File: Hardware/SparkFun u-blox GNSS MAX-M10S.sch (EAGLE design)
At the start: 45 parts, among them J1 USB-to-Serial, J2 Qwiic RA, J3 PTH, J4 Qwiic RA, U1 MAX-M10S

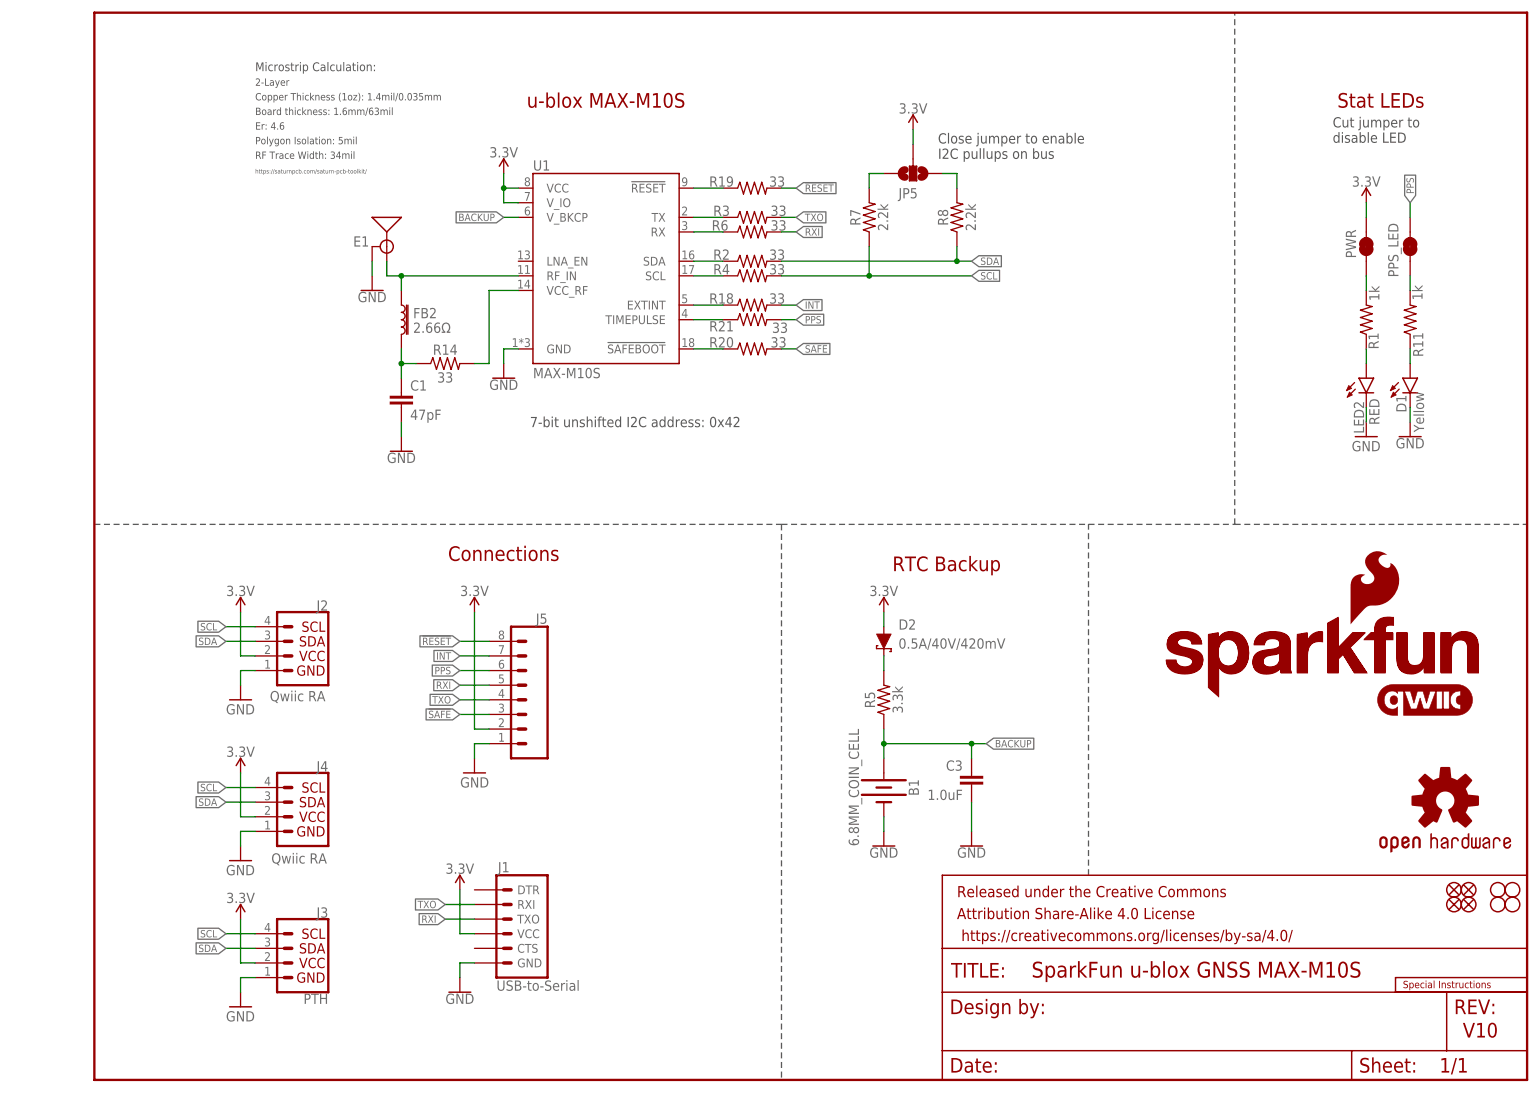
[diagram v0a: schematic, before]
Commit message: Changing RF path to 0402. Adding GND vias on both RF trace sides. Adding panel.
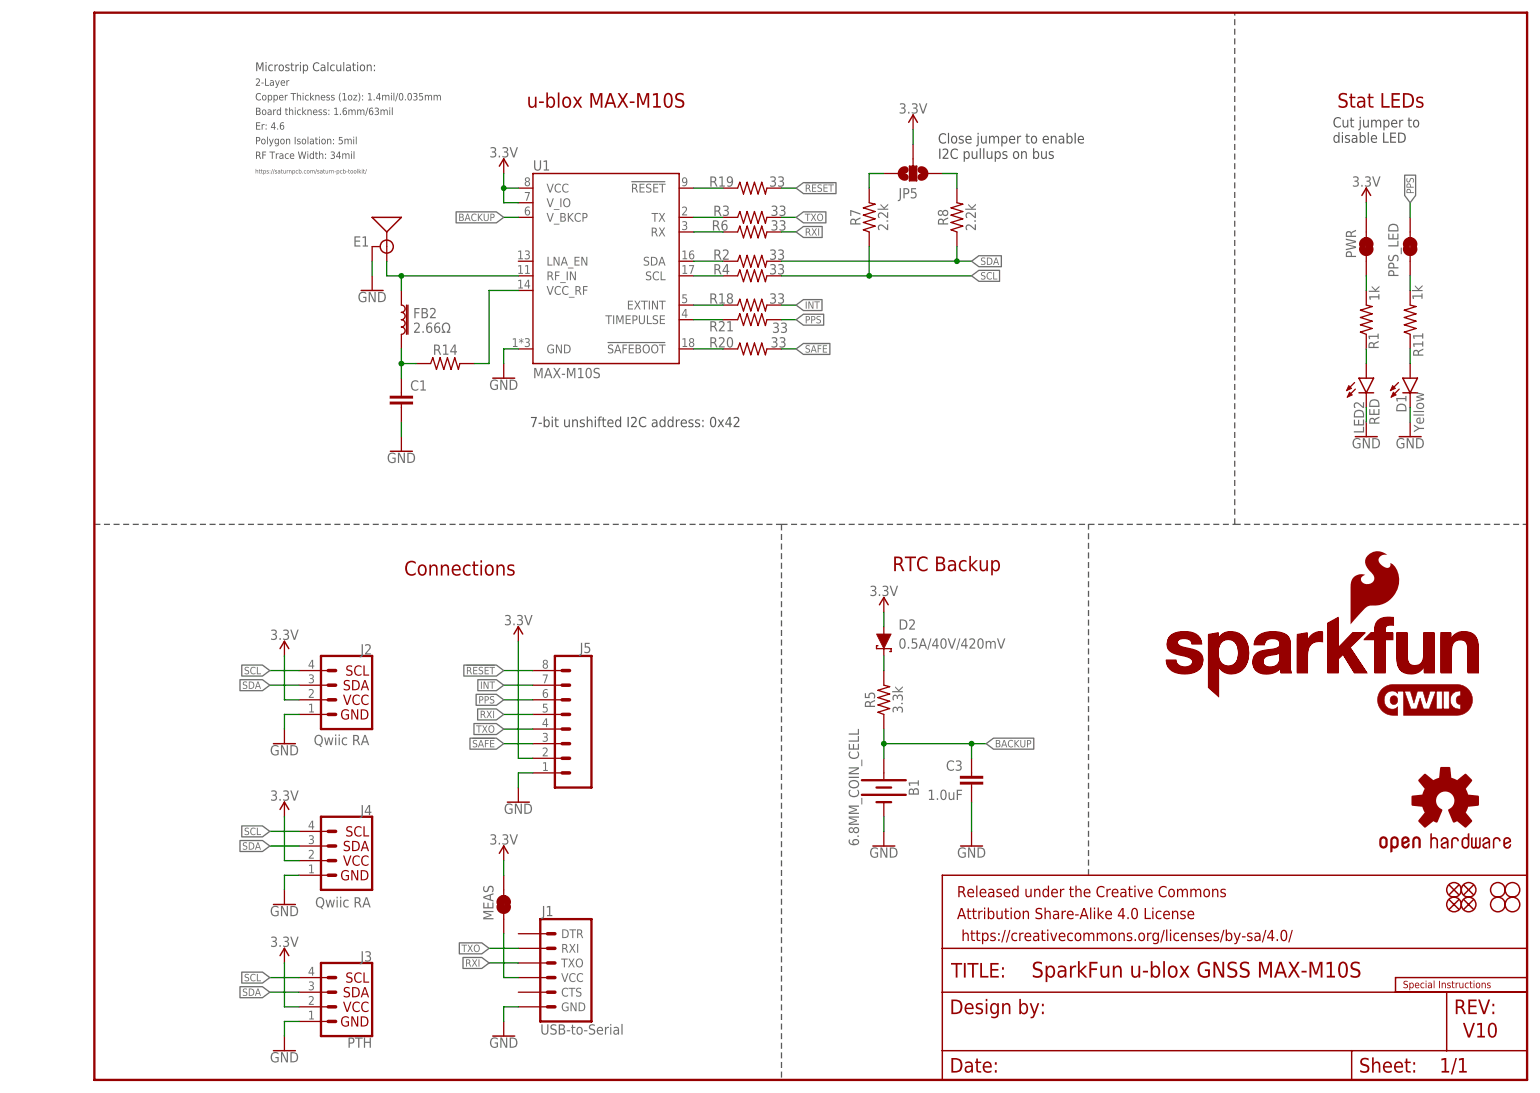
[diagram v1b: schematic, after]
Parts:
- added MEAS: JUMPER-COMBO_2_NC_TRACE, SparkFun-Jumpers:JUMPER-COMBO_2_NC_TRACE
- C1: value 47pF -> 47PF-0402_TIGHT-25V-5%-X7R; device SparkFun-Capacitors:47PF-0402-25V-5%-X7R -> SparkFun-Capacitors:47PF-0402_TIGHT-25V-5%-X7R
- R14: value 33 -> 33OHM-0402T-1/10W-1%; device SparkFun-Resistors:33OHM-0603-1/10W-1% -> SparkFun-Resistors:33OHM-0402T-1/10W-1%
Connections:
- new net N$1: J1.VCC, MEAS.1
- net 3.3V: now also MEAS.2; no longer J1.VCC
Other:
- moved on the sheet: J1, J2, J3, J4, J5

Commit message: Add ESD RF diode. Change to PTH SMA.
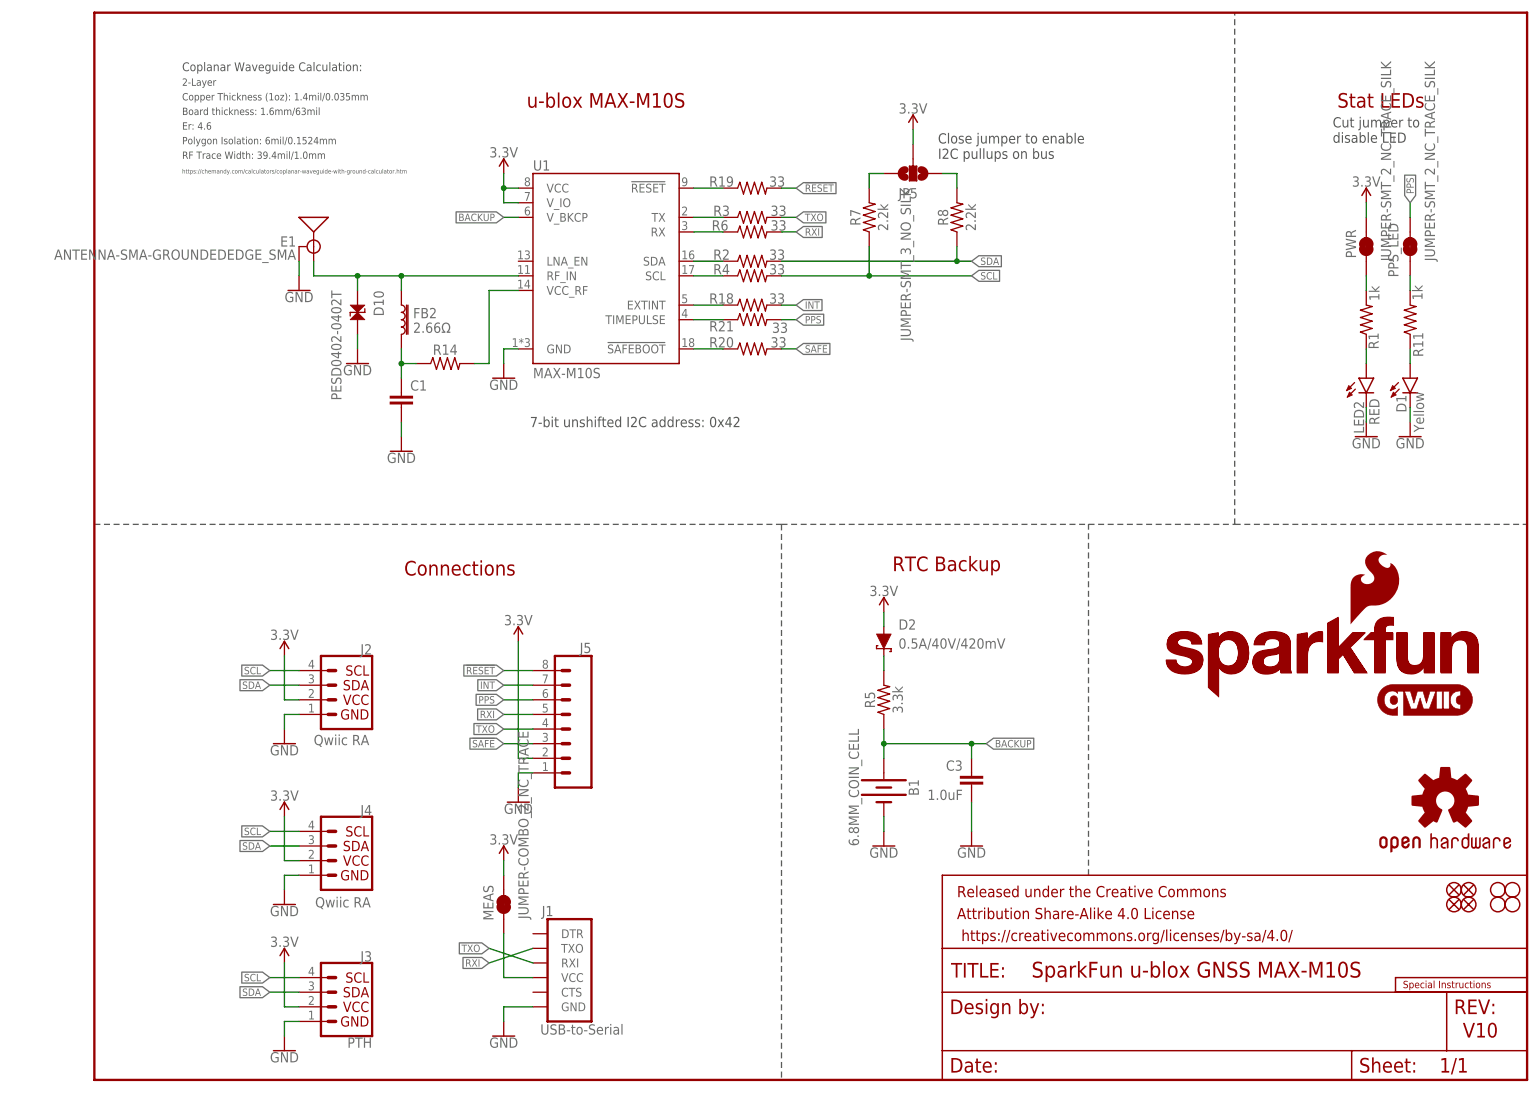
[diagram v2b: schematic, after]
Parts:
- added D10: PESD0402-0402T, SparkFun-DiscreteSemi:PESD0402-0402T
- C1: value 47PF-0402_TIGHT-25V-5%-X7R -> 47pF
- E1: value ANTENNA-SMA-GROUNDEDEDGE_SMA_SMD -> ANTENNA-SMA-GROUNDEDEDGE_SMA; device SparkFun-RF:ANTENNA-SMA-GROUNDEDEDGE_SMA_SMD -> SparkFun-RF:ANTENNA-SMA-GROUNDEDEDGE_SMA
- FB2: device SparkFun-Coils:FERRITE_BEAD-0402-2.66OHM-1GHZ -> SparkFun-Coils:FERRITE_BEAD-0402-2.66Ω-1GHZ
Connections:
- net GND: now also D10.2
- net GPS_RF: now also D10.1
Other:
- note added: "Coplanar Waveguide Calculation:"
- note added: "Polygon Isolation: 6mil/0.1524mm"
- note added: "RF Trace Width: 39.4mil/1.0mm"
- note added: "https://chemandy.com/calculators/coplanar-waveguide-with-ground-calculator.htm"
- note removed: "Microstrip Calculation:"
- note removed: "Polygon Isolation: 5mil"
- note removed: "RF Trace Width: 34mil"
- note removed: "https://saturnpcb.com/saturn-pcb-toolkit/"
- moved on the sheet: E1

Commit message: Add panel files
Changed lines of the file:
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@@
 <text x="237.744" y="7.366" size="2.54" layer="94">V10</text>
 <text x="93.98" y="114.3" size="1.778" layer="97" align="center">7-bit unshifted I2C address: 0x42</text>
-<text x="88.9" y="170.18" size="2.54" layer="94" ratio="15" rot="MR180" align="center">u-blox MAX-M10S</text>
-<text x="148.082" y="89.662" size="2.54" layer="94" ratio="15" rot="MR180" align="center">RTC Backup</text>
-<text x="223.52" y="170.18" size="2.54" layer="94" ratio="15" rot="MR180" align="center">Stat LEDs</text>
+<text x="88.9" y="170.18" size="2.54" layer="94" rot="MR180" align="center">u-blox MAX-M10S</text>
+<text x="148.082" y="89.662" size="2.54" layer="94" rot="MR180" align="center">RTC Backup</text>
+<text x="223.52" y="170.18" size="2.54" layer="94" rot="MR180" align="center">Stat LEDs</text>
 <text x="146.558" y="160.02" size="1.778" layer="97">Close jumper to enable
 I2C pullups on bus</text>
@@
 disable LED</text>
 <text x="15.24" y="175.26" size="1.524" layer="97" ratio="15">Coplanar Waveguide Calculation:</text>
-<text x="63.5" y="88.9" size="2.54" layer="94" ratio="15" rot="MR180" align="center">Connections</text>
+<text x="63.5" y="88.9" size="2.54" layer="94" rot="MR180" align="center">Connections</text>
 <wire x1="119.38" y1="96.52" x2="119.38" y2="0" width="0.2032" layer="97" style="longdash"/>
 <wire x1="0" y1="96.52" x2="119.38" y2="96.52" width="0.2032" layer="97" style="longdash"/>
@@
 <instance part="JP5" gate="G$1" x="142.24" y="157.48" smashed="yes" rot="R270">
 <attribute name="NAME" x="139.7" y="153.162" size="1.778" layer="95" font="vector"/>
-<attribute name="VALUE" x="141.859" y="154.94" size="1.778" layer="96" font="vector" rot="R270" align="top-left"/>
 </instance>
 <instance part="SUPPLY9" gate="G$1" x="142.24" y="165.1" smashed="yes">
@@
 <instance part="PPS_LED" gate="G$1" x="228.6" y="144.78" smashed="yes" rot="R90">
 <attribute name="NAME" x="226.568" y="139.446" size="1.778" layer="95" font="vector" rot="R90"/>
-<attribute name="VALUE" x="231.14" y="142.24" size="1.778" layer="96" font="vector" rot="R90" align="top-left"/>
 </instance>
 <instance part="D2" gate="G$1" x="137.16" y="76.2" smashed="yes" rot="R270">
@@
 <instance part="PWR" gate="G$1" x="220.98" y="144.78" smashed="yes" rot="R90">
 <attribute name="NAME" x="219.202" y="142.748" size="1.778" layer="95" font="vector" rot="R90"/>
-<attribute name="VALUE" x="223.52" y="142.24" size="1.778" layer="96" font="vector" rot="R90" align="top-left"/>
 </instance>
 <instance part="U1" gate="U1" x="88.9" y="142.24" smashed="yes">
@@
 <instance part="E1" gate="G$1" x="38.1" y="144.78" smashed="yes" rot="MR0">
 <attribute name="NAME" x="35.052" y="144.78" size="1.778" layer="95" font="vector" rot="MR0"/>
-<attribute name="VALUE" x="35.052" y="142.494" size="1.778" layer="96" font="vector" rot="MR0"/>
 </instance>
 <instance part="J5" gate="G$1" x="81.28" y="60.96" smashed="yes" rot="MR0">
@@
 <instance part="MEAS" gate="JP1" x="71.12" y="30.48" smashed="yes" rot="R90">
 <attribute name="NAME" x="69.342" y="27.686" size="1.778" layer="95" font="vector" rot="R90"/>
-<attribute name="VALUE" x="73.66" y="27.94" size="1.778" layer="96" font="vector" rot="R90" align="top-left"/>
 </instance>
 <instance part="SUPPLY2" gate="G$1" x="33.02" y="73.66" smashed="yes">
@@
 <segment>
 <pinref part="J1" gate="G$1" pin="TXO"/>
-<wire x1="76.2" y1="22.86" x2="68.58" y2="20.32" width="0.1524" layer="91"/>
-<label x="68.58" y="20.32" size="1.27" layer="95" rot="R180" xref="yes"/>
+<wire x1="76.2" y1="22.86" x2="68.58" y2="22.86" width="0.1524" layer="91"/>
+<label x="68.58" y="22.86" size="1.27" layer="95" rot="R180" xref="yes"/>
 </segment>
 </net>
@@
 <segment>
 <pinref part="J1" gate="G$1" pin="RXI"/>
-<wire x1="76.2" y1="20.32" x2="68.58" y2="22.86" width="0.1524" layer="91"/>
-<label x="68.58" y="22.86" size="1.27" layer="95" rot="R180" xref="yes"/>
-</segment>
-</net>
+<wire x1="76.2" y1="20.32" x2="68.58" y2="20.32" width="0.1524" layer="91"/>
+<label x="68.58" y="20.32" size="1.27" layer="95" rot="R180" xref="yes"/>
+</segment>
+</net>
